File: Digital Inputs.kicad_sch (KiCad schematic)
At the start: 54 parts, among them U2 LMH6611, U3 LMH6611, U4 LMH6611, U5 LMH6611, U6 LMH6611, U7 LMH6611

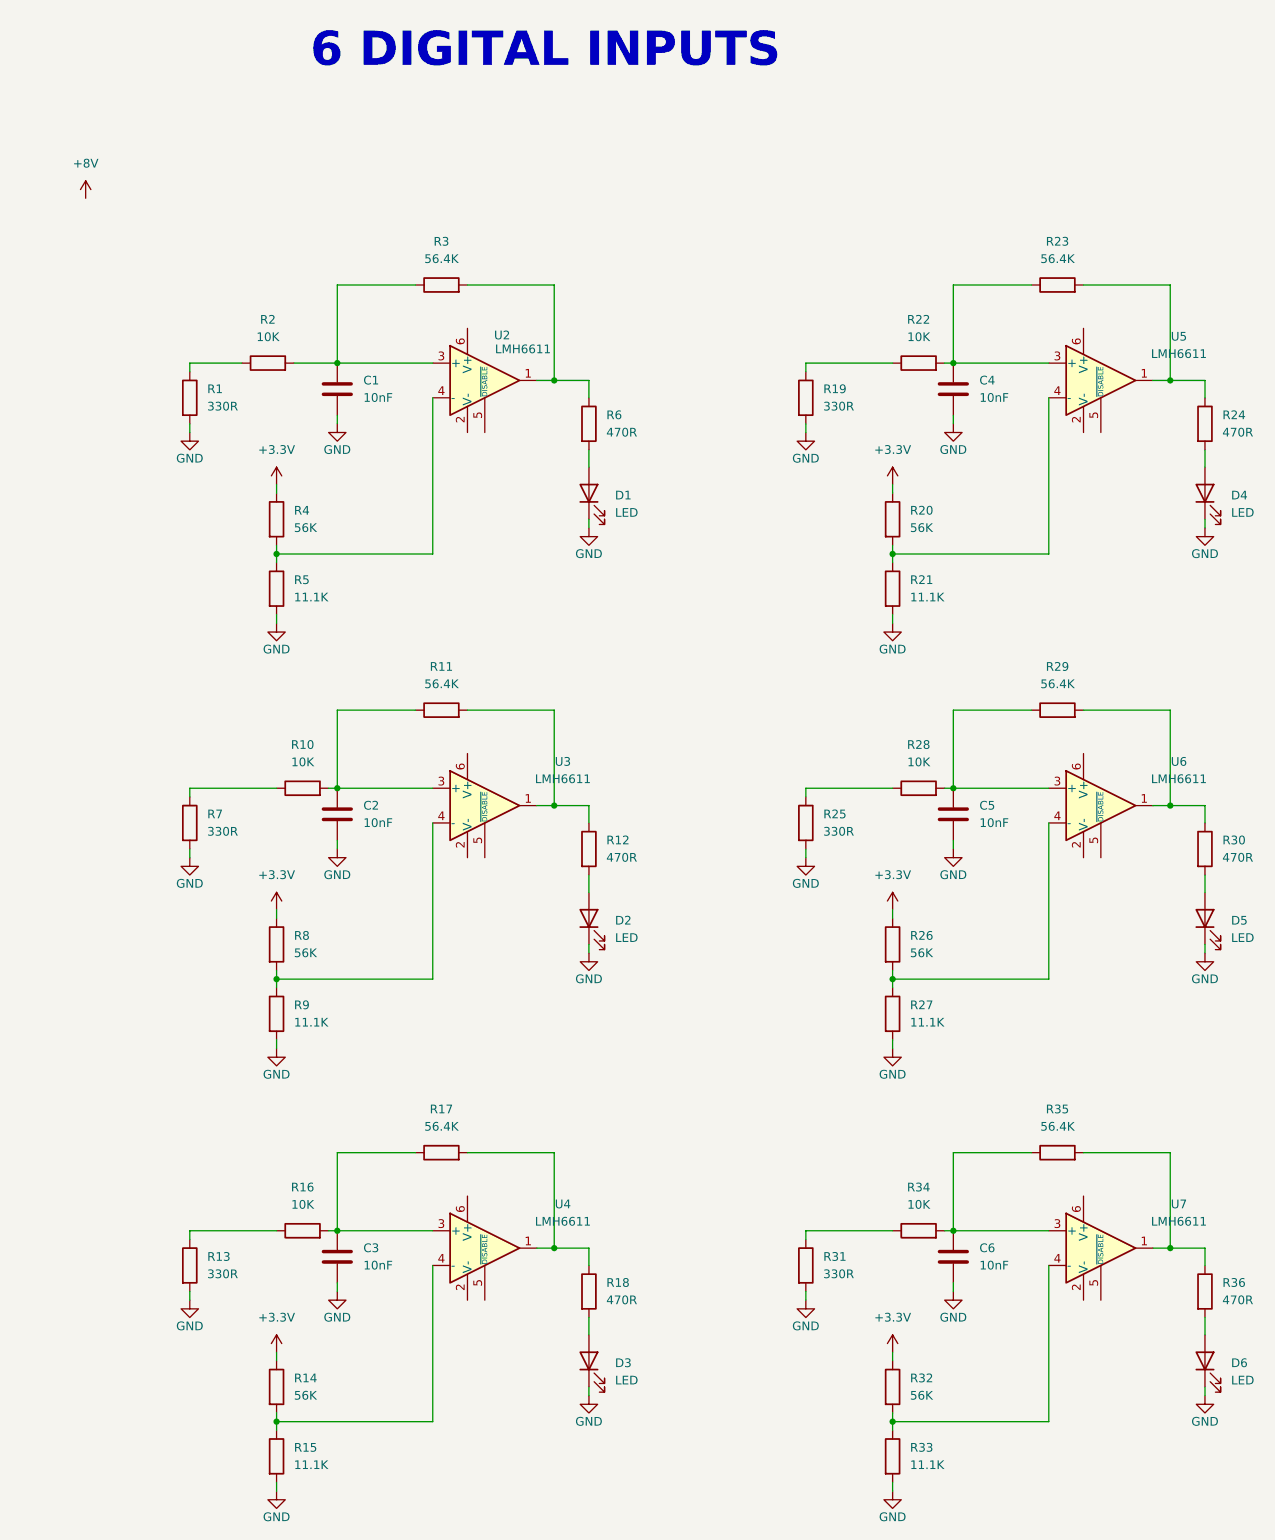
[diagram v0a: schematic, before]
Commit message: Se termina el circuito de entrada análoga, se escoge la bornera. Se termina las salidas de rele, se asumen que se trabajara maximo a 220V y solo para activar contactores. El circuito para el sensor namur se esta realizando
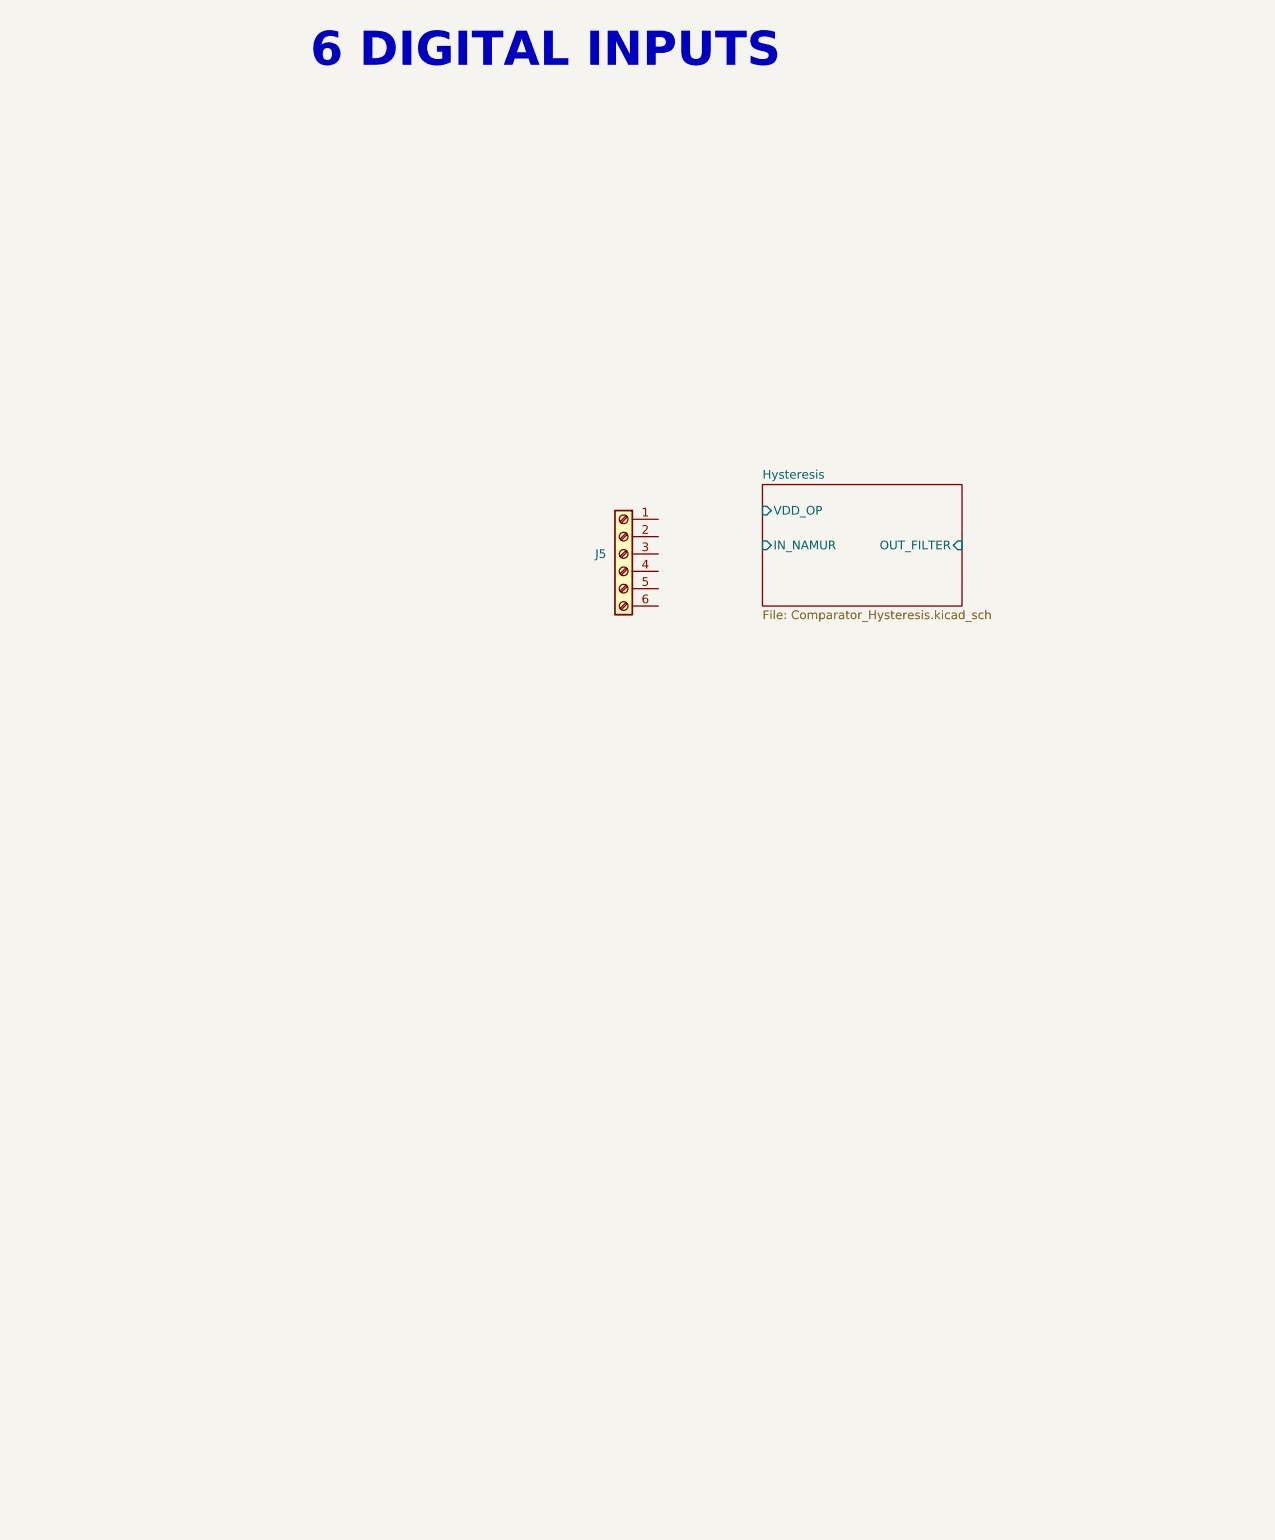
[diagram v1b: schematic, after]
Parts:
- removed C1, C2, C3, C4, C5, C6: 10nF, symbol Device:C
- removed D1, D2, D3, D4, D5, D6: LED, symbol Device:LED
- removed R1, R13, R19, R25, R31, R7: 330R, symbol 1-Resistor:R
- removed R10, R16, R2, R22, R28, R34: 10K, symbol 1-Resistor:R
- removed R11, R17, R23, R29, R3, R35: 56.4K, symbol 1-Resistor:R
- removed R12, R18, R24, R30, R36, R6: 470R, symbol 1-Resistor:R
- removed R14, R20, R26, R32, R4, R8: 56K, symbol 1-Resistor:R
- removed R15, R21, R27, R33, R5, R9: 11.1K, symbol 1-Resistor:R
- removed U2, U3, U4, U5, U6, U7: LMH6611, Package_TO_SOT_SMD:TSOT-23-6, symbol Amplifier_Operational:LMH6611
- added J5: Screw_Terminal_01x06, LIB_PCB_CONT:15EDGRC_6P_3.81mm_Male-Rect_Degson, symbol Connector:Screw_Terminal_01x06
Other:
- added sheet Hysteresis (Comparator_Hysteresis.kicad_sch)

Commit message: Avance
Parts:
- added J6, J7: Screw_Terminal_01x06, LIB_PCB_CONT:15EDGRC_6P_3.81mm_Male-Rect_Degson, symbol Connector:Screw_Terminal_01x06
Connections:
- net 8V2: now reaches J5.1 (Pin_1)
- net 8V2: now also J5.3 (Pin_3), J5.5 (Pin_5), J6.1 (Pin_1), J6.3 (Pin_3), J6.5 (Pin_5), J7.1 (Pin_1), J7.3 (Pin_3), J7.5 (Pin_5)
- net NAMUR_1: now reaches J5.2 (Pin_2)
- net NAMUR_2: now reaches J5.4 (Pin_4)
- net NAMUR_3: now reaches J5.6 (Pin_6)
- new net NAMUR_4: J6.2 (Pin_2)
- new net NAMUR_5: J6.4 (Pin_4)
- new net NAMUR_6: J6.6 (Pin_6)
- new net NAMUR_7: J7.2 (Pin_2)
- new net NAMUR_8: J7.4 (Pin_4)
- new net NAMUR_9: J7.6 (Pin_6)
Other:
- added sheet Hysteresis1 (Comparator_Hysteresis.kicad_sch)
- added sheet Hysteresis2 (Comparator_Hysteresis.kicad_sch)
- added sheet Hysteresis3 (Comparator_Hysteresis.kicad_sch)
- added sheet Hysteresis4 (Comparator_Hysteresis.kicad_sch)
- added sheet Hysteresis5 (Comparator_Hysteresis.kicad_sch)
- added sheet Hysteresis6 (Comparator_Hysteresis.kicad_sch)
- added sheet Hysteresis7 (Comparator_Hysteresis.kicad_sch)
- added sheet Hysteresis8 (Comparator_Hysteresis.kicad_sch)
- moved on the sheet: J5

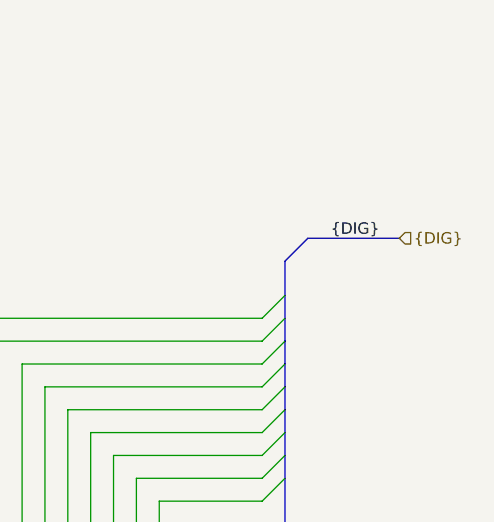
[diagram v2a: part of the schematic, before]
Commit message: avance de pcb, se considera borneras externas para conexión de alimentación
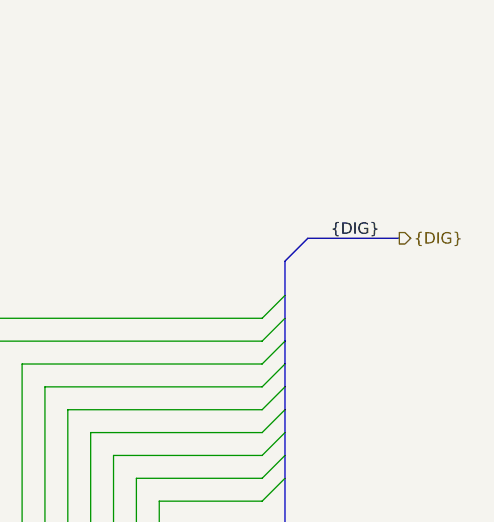
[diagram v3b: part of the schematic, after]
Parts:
- J5, J6, J7: footprint LIB_PCB_CONT:15EDGRC_6P_3.81mm_Male-Rect_Degson -> LIB_PCB_CONT:15EDGVC_6P_3.81mm_Male-Vert_Degson
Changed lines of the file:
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@@
 	)
 	(hierarchical_label "{DIG}"
-		(shape input)
+		(shape output)
 		(at 203.2 52.07 0)
 		(effects
@@
 			)
 		)
-		(property "Footprint" "LIB_PCB_CONT:15EDGRC_6P_3.81mm_Male-Rect_Degson"
+		(property "Footprint" "LIB_PCB_CONT:15EDGVC_6P_3.81mm_Male-Vert_Degson"
 			(at 49.53 80.01 0)
 			(effects
@@
 			)
 		)
-		(property "Footprint" "LIB_PCB_CONT:15EDGRC_6P_3.81mm_Male-Rect_Degson"
+		(property "Footprint" "LIB_PCB_CONT:15EDGVC_6P_3.81mm_Male-Vert_Degson"
 			(at 49.53 63.5 0)
 			(effects
@@
 			)
 		)
-		(property "Footprint" "LIB_PCB_CONT:15EDGRC_6P_3.81mm_Male-Rect_Degson"
+		(property "Footprint" "LIB_PCB_CONT:15EDGVC_6P_3.81mm_Male-Vert_Degson"
 			(at 49.53 97.79 0)
 			(effects

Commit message: Avance del posicionamiento
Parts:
- removed J7: Screw_Terminal_01x06, LIB_PCB_CONT:15EDGVC_6P_3.81mm_Male-Vert_Degson, symbol Connector:Screw_Terminal_01x06
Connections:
- net 8V2: now also J5.2 (Pin_2); no longer J5.3 (Pin_3), J5.5 (Pin_5), J6.1 (Pin_1), J6.3 (Pin_3), J6.5 (Pin_5)
- net NAMUR_1: now also J5.4 (Pin_4); no longer J5.2 (Pin_2)
- net NAMUR_2: now also J5.5 (Pin_5); no longer J5.4 (Pin_4)
- net NAMUR_4: now also J6.1 (Pin_1); no longer J6.2 (Pin_2)
- net NAMUR_5: now also J6.2 (Pin_2); no longer J6.4 (Pin_4)
- net NAMUR_6: now also J6.3 (Pin_3); no longer J6.6 (Pin_6)
- net NAMUR_7: now also J6.4 (Pin_4)
- net NAMUR_8: now also J6.5 (Pin_5)
- net NAMUR_9: now also J6.6 (Pin_6)
- new net GND: J5.3 (Pin_3)
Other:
- moved on the sheet: J5, J6

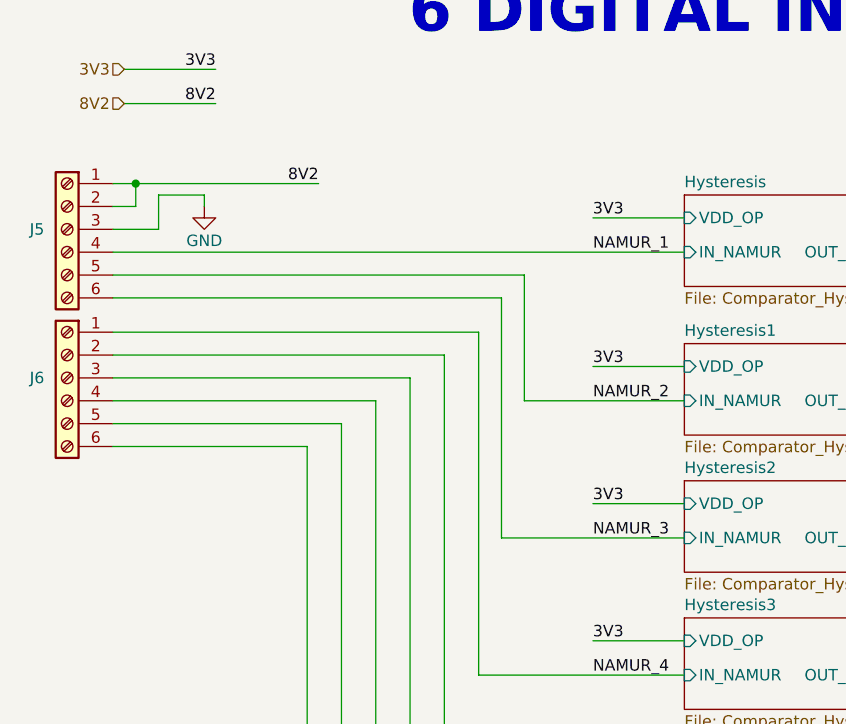
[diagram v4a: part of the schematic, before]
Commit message: Se empieza a evaluar la conexión del ethernet con la carcasa, parte analog, dig y micro en posición, tambien se busca solución para la salida de led de las entradas digitales
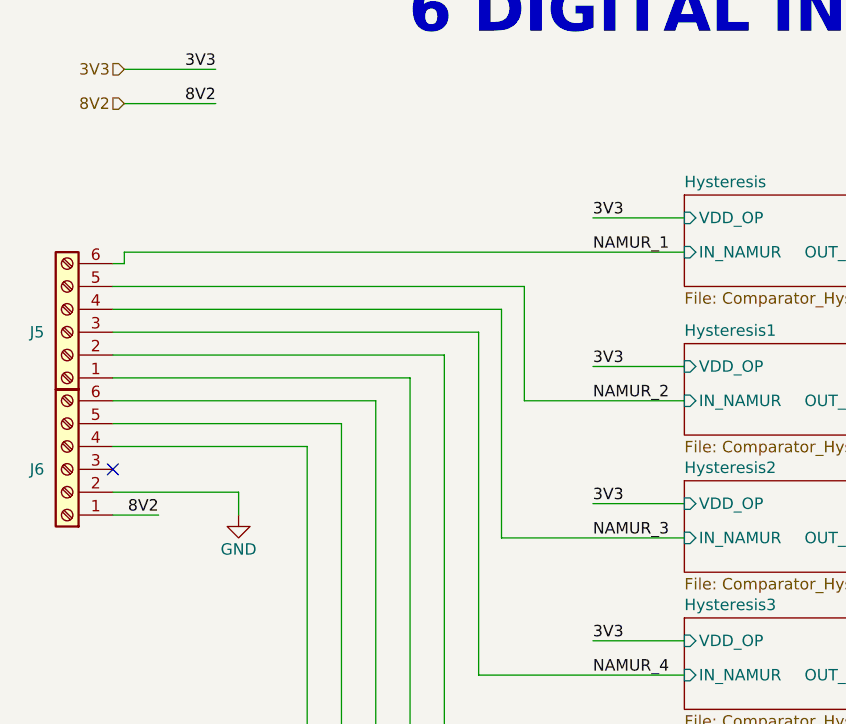
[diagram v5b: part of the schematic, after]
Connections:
- net 8V2: now also J6.1 (Pin_1); no longer J5.1 (Pin_1), J5.2 (Pin_2)
- net GND: now also J6.2 (Pin_2); no longer J5.3 (Pin_3)
- net NAMUR_1: now also J5.6 (Pin_6); no longer J5.4 (Pin_4)
- net NAMUR_3: now also J5.4 (Pin_4); no longer J5.6 (Pin_6)
- net NAMUR_4: now also J5.3 (Pin_3); no longer J6.1 (Pin_1)
- net NAMUR_5: now also J5.2 (Pin_2); no longer J6.2 (Pin_2)
- net NAMUR_6: now also J5.1 (Pin_1); no longer J6.3 (Pin_3)
- net NAMUR_7: now also J6.6 (Pin_6); no longer J6.4 (Pin_4)
- net NAMUR_9: now also J6.4 (Pin_4); no longer J6.6 (Pin_6)
- no-connect marks 0 -> 1
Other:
- moved on the sheet: J5, J6
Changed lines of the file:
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@@
 		)
 	)
-	(junction
-		(at 53.34 52.07)
-		(diameter 0)
-		(color 0 0 0 0)
+	(no_connect
+		(at 50.8 83.82)
 	)
 	(bus_entry
@@
 	(wire
 		(pts
-			(xy 50.8 59.69) (xy 114.3 59.69)
+			(xy 50.8 60.96) (xy 52.07 60.96)
 		)
 		(stroke
@@
 		)
 	)
-	(wire
-		(pts
-			(xy 55.88 53.34) (xy 55.88 57.15)
-		)
-		(stroke
-			(width 0)
-			(type default)
-		)
-	)
 	(bus
 		(pts
@@
 	(wire
 		(pts
-			(xy 60.96 54.61) (xy 60.96 53.34)
+			(xy 64.77 88.9) (xy 64.77 86.36)
 		)
 		(stroke
@@
 	(wire
 		(pts
-			(xy 50.8 64.77) (xy 93.98 64.77)
+			(xy 50.8 66.04) (xy 93.98 66.04)
 		)
 		(stroke
@@
 	(wire
 		(pts
-			(xy 93.98 64.77) (xy 93.98 91.44)
+			(xy 93.98 66.04) (xy 93.98 91.44)
 		)
 		(stroke
@@
 		)
 	)
-	(wire
-		(pts
-			(xy 55.88 57.15) (xy 50.8 57.15)
-		)
-		(stroke
-			(width 0)
-			(type default)
-		)
-	)
 	(bus
 		(pts
@@
 	(wire
 		(pts
-			(xy 50.8 52.07) (xy 53.34 52.07)
-		)
-		(stroke
-			(width 0)
-			(type default)
-		)
-	)
-	(wire
-		(pts
 			(xy 104.14 165.1) (xy 114.3 165.1)
 		)
@@
 	(wire
 		(pts
+			(xy 50.8 86.36) (xy 64.77 86.36)
+		)
+		(stroke
+			(width 0)
+			(type default)
+		)
+	)
+	(wire
+		(pts
 			(xy 158.75 63.5) (xy 158.75 76.2)
 		)
@@
 	(wire
 		(pts
-			(xy 96.52 62.23) (xy 96.52 76.2)
+			(xy 96.52 63.5) (xy 96.52 76.2)
 		)
 		(stroke
@@
 	(wire
 		(pts
-			(xy 53.34 52.07) (xy 73.66 52.07)
+			(xy 50.8 88.9) (xy 55.88 88.9)
 		)
 		(stroke
@@
 	(wire
 		(pts
-			(xy 50.8 54.61) (xy 53.34 54.61)
-		)
-		(stroke
-			(width 0)
-			(type default)
-		)
-	)
-	(wire
-		(pts
 			(xy 50.8 76.2) (xy 80.01 76.2)
 		)
@@
 		)
 	)
+	(wire
+		(pts
+			(xy 52.07 59.69) (xy 114.3 59.69)
+		)
+		(stroke
+			(width 0)
+			(type default)
+		)
+	)
 	(bus
 		(pts
@@
 	(wire
 		(pts
-			(xy 60.96 53.34) (xy 55.88 53.34)
-		)
-		(stroke
-			(width 0)
-			(type default)
-		)
-	)
-	(wire
-		(pts
 			(xy 161.29 66.04) (xy 161.29 91.44)
 		)
@@
 	(wire
 		(pts
-			(xy 53.34 54.61) (xy 53.34 52.07)
-		)
-		(stroke
-			(width 0)
-			(type default)
-		)
-	)
-	(wire
-		(pts
 			(xy 168.91 73.66) (xy 187.96 73.66)
 		)
@@
 	(wire
 		(pts
-			(xy 50.8 62.23) (xy 96.52 62.23)
+			(xy 50.8 63.5) (xy 96.52 63.5)
 		)
 		(stroke
@@
 		(pts
 			(xy 163.83 106.68) (xy 163.83 68.58)
+		)
+		(stroke
+			(width 0)
+			(type default)
+		)
+	)
+	(wire
+		(pts
+			(xy 52.07 60.96) (xy 52.07 59.69)
 		)
 		(stroke
@@
 	)
 	(label "8V2"
-		(at 73.66 52.07 180)
+		(at 55.88 88.9 180)
 		(effects
 			(font
@@
 	(symbol
 		(lib_id "Connector:Screw_Terminal_01x06")
-		(at 45.72 73.66 0)
-		(mirror y)
+		(at 45.72 83.82 180)
 		(unit 1)
 		(exclude_from_sim no)
@@
 		(dnp no)
 		(property "Reference" "J6"
-			(at 43.18 73.6599 0)
+			(at 43.18 83.8201 0)
 			(effects
 				(font
@@
 		)
 		(property "Value" "Screw_Terminal_01x06"
-			(at 43.18 76.1999 0)
+			(at 43.18 81.2801 0)
 			(effects
 				(font
@@
 		)
 		(property "Footprint" "LIB_PCB_CONT:15EDGVC_6P_3.81mm_Male-Vert_Degson"
-			(at 45.72 73.66 0)
+			(at 45.72 83.82 0)
 			(effects
 				(font
@@
 		)
 		(property "Datasheet" "~"
-			(at 45.72 73.66 0)
+			(at 45.72 83.82 0)
 			(effects
 				(font
@@
 		)
 		(property "Description" "Generic screw terminal, single row, 01x06, script generated (kicad-library-utils/schlib/autogen/connector/)"
-			(at 45.72 73.66 0)
+			(at 45.72 83.82 0)
 			(effects
 				(font
@@
 	(symbol
 		(lib_id "Connector:Screw_Terminal_01x06")
-		(at 45.72 57.15 0)
-		(mirror y)
+		(at 45.72 68.58 180)
 		(unit 1)
 		(exclude_from_sim no)
@@
 		(dnp no)
 		(property "Reference" "J5"
-			(at 43.18 57.1499 0)
+			(at 43.18 68.5801 0)
 			(effects
 				(font
@@
 		)
 		(property "Value" "Screw_Terminal_01x06"
-			(at 43.18 59.6899 0)
+			(at 43.18 66.0401 0)
 			(effects
 				(font
@@
 		)
 		(property "Footprint" "LIB_PCB_CONT:15EDGVC_6P_3.81mm_Male-Vert_Degson"
-			(at 45.72 57.15 0)
+			(at 45.72 68.58 0)
 			(effects
 				(font
@@
 		)
 		(property "Datasheet" "~"
-			(at 45.72 57.15 0)
+			(at 45.72 68.58 0)
 			(effects
 				(font
@@
 		)
 		(property "Description" "Generic screw terminal, single row, 01x06, script generated (kicad-library-utils/schlib/autogen/connector/)"
-			(at 45.72 57.15 0)
+			(at 45.72 68.58 0)
 			(effects
 				(font
@@
 	(symbol
 		(lib_id "power:GND")
-		(at 60.96 54.61 0)
+		(at 64.77 88.9 0)
 		(unit 1)
 		(exclude_from_sim no)
@@
 		(dnp no)
 		(property "Reference" "#PWR0117"
-			(at 60.96 60.96 0)
+			(at 64.77 95.25 0)
 			(effects
 				(font
@@
 		)
 		(property "Value" "GND"
-			(at 60.96 58.42 0)
+			(at 64.77 92.71 0)
 			(effects
 				(font
@@
 		)
 		(property "Footprint" ""
-			(at 60.96 54.61 0)
+			(at 64.77 88.9 0)
 			(effects
 				(font
@@
 		)
 		(property "Datasheet" ""
-			(at 60.96 54.61 0)
+			(at 64.77 88.9 0)
 			(effects
 				(font
@@
 		)
 		(property "Description" "Power symbol creates a global label with name \"GND\" , ground"
-			(at 60.96 54.61 0)
-			(effects
-				(font
+			(at 64.77 88.9 0)
+			(effects
+				(font
